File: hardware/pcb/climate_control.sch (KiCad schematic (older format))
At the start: 27 parts

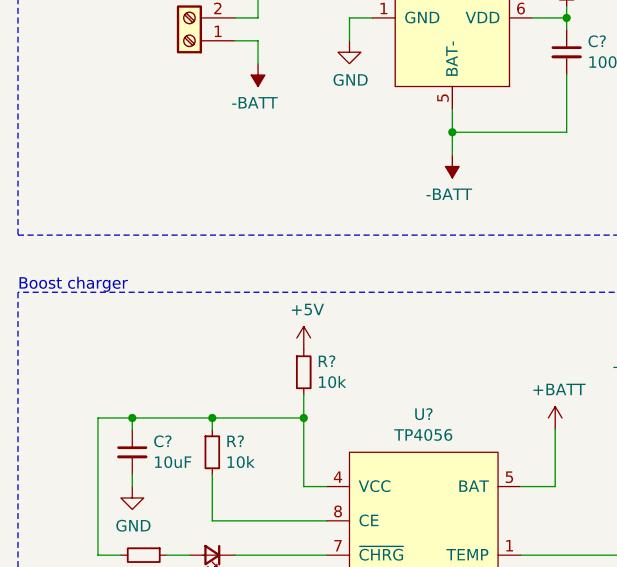
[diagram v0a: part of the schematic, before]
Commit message: Correct title on battery charger.
Wrote boost before, when it is a buck charger. Now corrected.
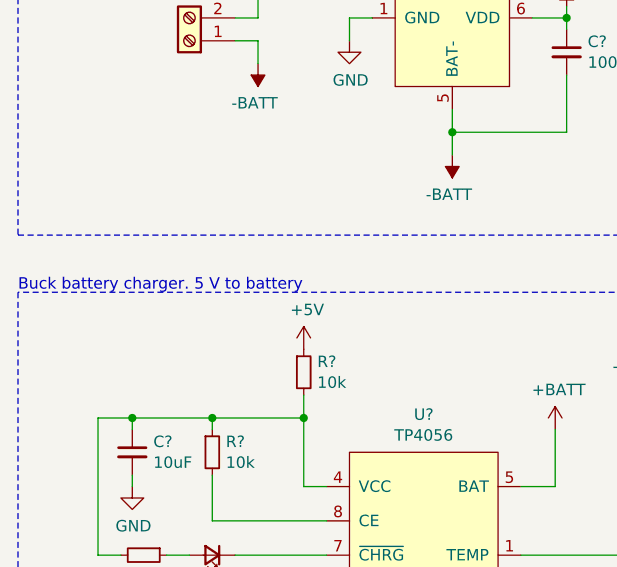
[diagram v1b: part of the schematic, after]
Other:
- note added: "Buck battery charger. 5 V to battery"
- note removed: "Boost charger"
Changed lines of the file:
@@
 	1200 3300 1550 3300
 Text Notes 700  2750 0    50   ~ 0
-Boost charger
+Buck battery charger. 5 V to battery
 Wire Notes Line
 	700  5100 700  7650

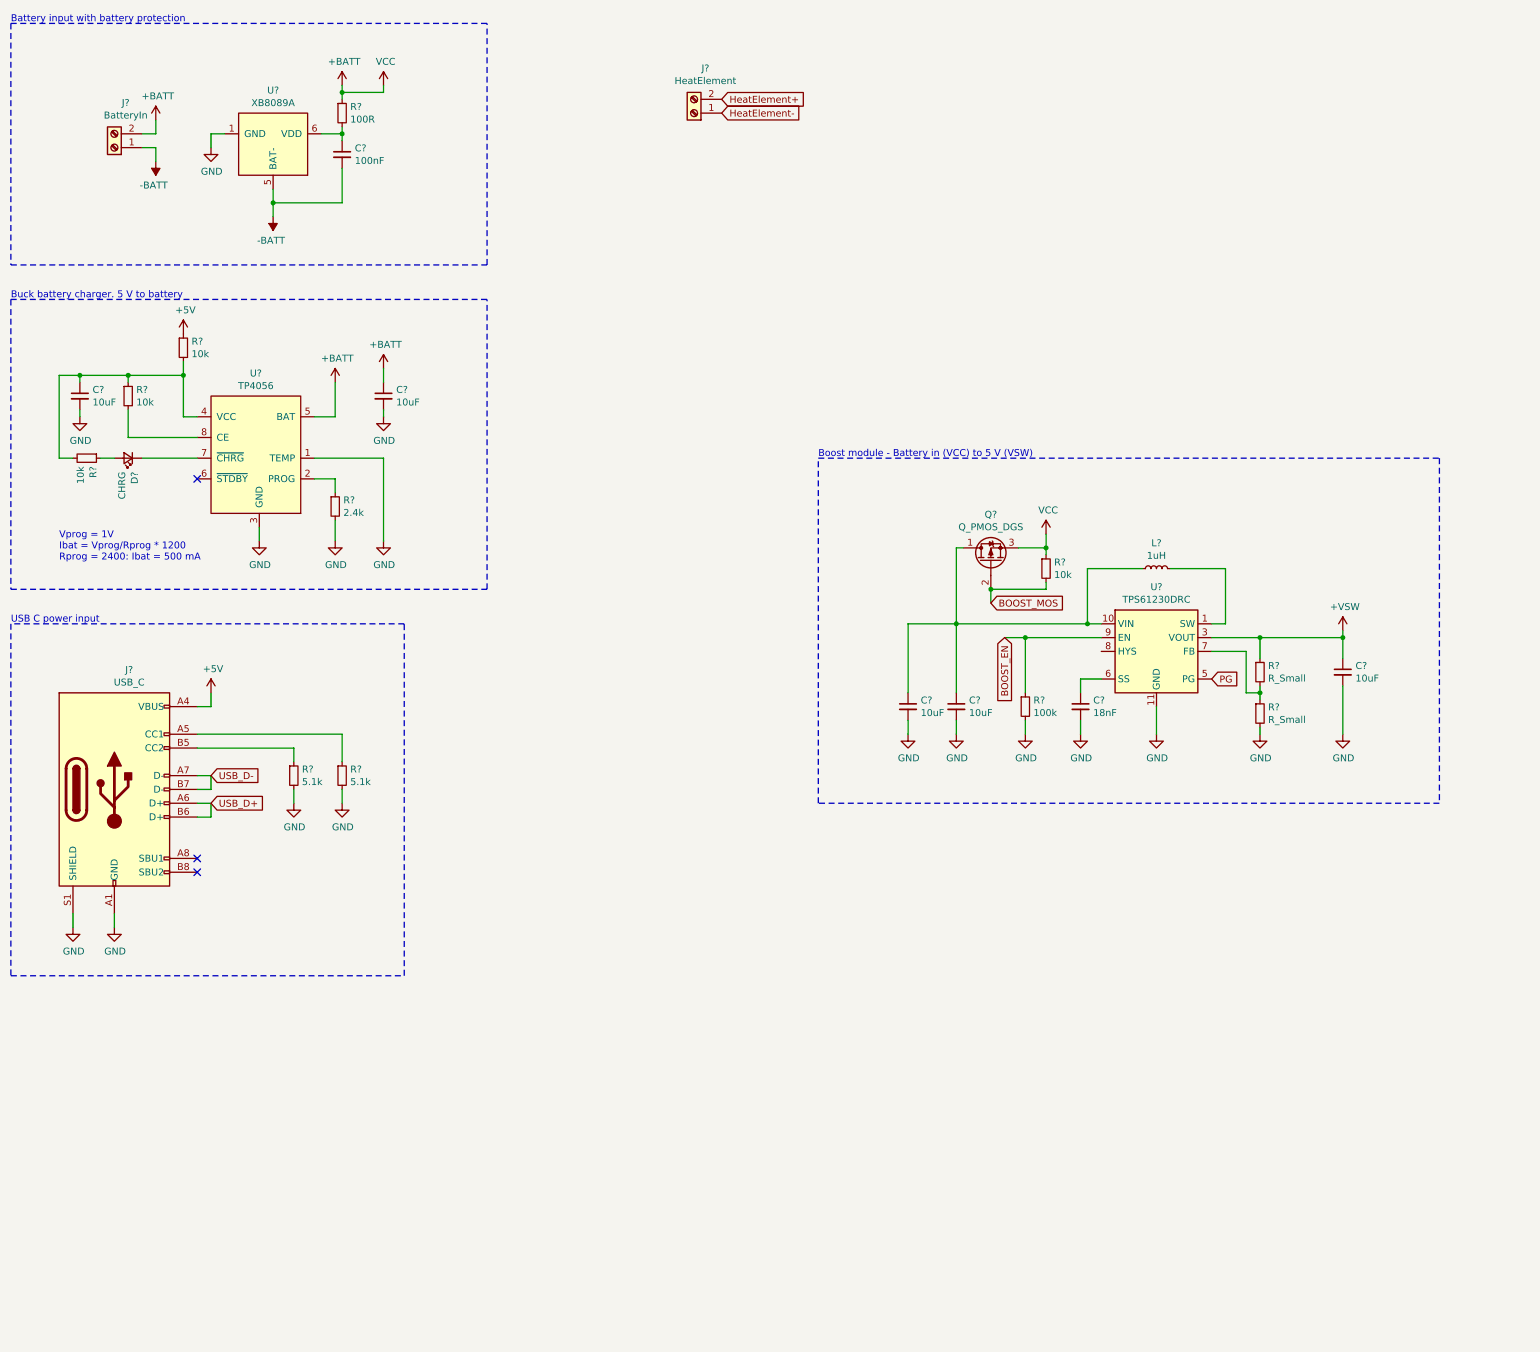
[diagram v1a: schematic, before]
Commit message: Added MCU and better control.
MCU with all connection is added.
Output to heater now has a mosfet to PWM to.
LED Switch has a connection with mosfet to control LED.
LED Switch has a LP filter for debounce purpose.
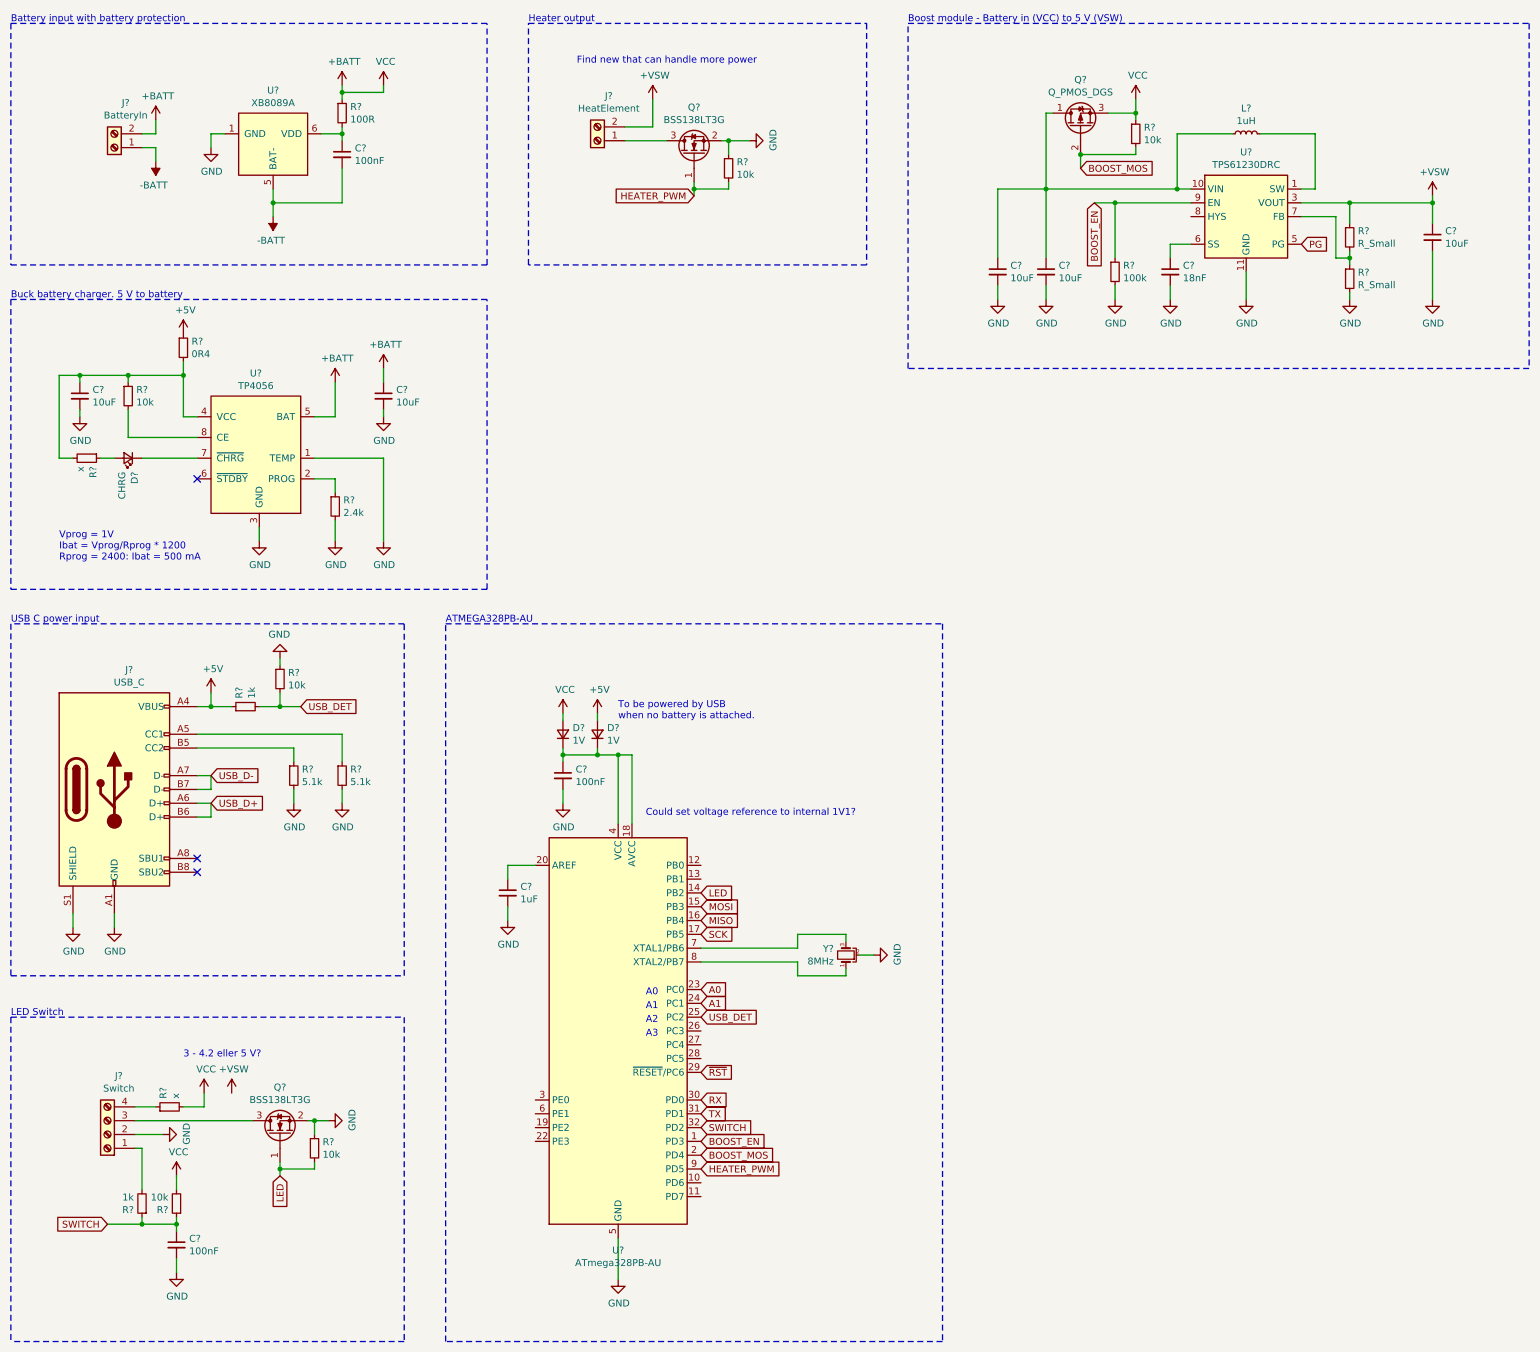
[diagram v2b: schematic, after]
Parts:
- added C? (x2): 100nF, symbol Device:C_Small
- added C?: 1uF, symbol Device:C_Small
- added D? (x2): 1V, symbol Device:D_Small
- added J?: Switch, symbol Connector:Screw_Terminal_01x04
- added Q? (x2): BSS138LT3G, symbol Device:Q_NMOS_GSD
- added R?: x, symbol Device:R_Small
- added R? (x4): 10k, symbol Device:R_Small
- added R? (x2): 1k, symbol Device:R_Small
- added U?: ATmega328PB-AU, Package_QFP:TQFP-32_7x7mm_P0.8mm, symbol climate_control:ATmega328PB-AU
- added Y?: 8MHz, symbol Device:Crystal_GND2_Small
- R?: value 10k -> x
- R?: value 10k -> 0R4
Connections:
- net HeatElement+ is gone; now on net +VSW: J?.2 (Pin_2)
- net +5V: now also D?.2 (A), R?.1
- net +BATT: now also D?.2 (A), R?.2, R?.2
- net BOOST_EN: now also U?.1 (PD3)
- net BOOST_MOS: now also U?.2 (PD4)
- net GND: now also C?.2, C?.2, C?.2, J?.2 (Pin_2), Q?.2 (S), Q?.2 (S), R?.1, R?.1, R?.1, U?.21 (GND), U?.5 (GND), Y?.2
- net HeatElement-: no longer names the net of J?.1 (Pin_1)
- net HeatElement-: now also Q?.3 (D)
- new net: C?.1, D?.1 (K), D?.1 (K), U?.18 (AVCC), U?.4 (VCC)
- new net: C?.1, U?.20 (AREF)
- new net: U?.7 (XTAL1/PB6), Y?.3
- new net: U?.8 (XTAL2/PB7), Y?.1
- new net: J?.1 (Pin_1), R?.2
- new net: J?.3 (Pin_3), Q?.3 (D)
- new net: J?.4 (Pin_4), R?.1
- new net A0: U?.23 (PC0)
- new net A1: U?.24 (PC1)
- new net HEATER_PWM: Q?.1 (G), R?.2, U?.9 (PD5)
- new net LED: Q?.1 (G), R?.2, U?.14 (PB2)
- new net MISO: U?.16 (PB4)
- new net MOSI: U?.15 (PB3)
- new net RX: U?.30 (PD0)
- new net SCK: U?.17 (PB5)
- new net SWITCH: C?.1, R?.1, R?.1, U?.32 (PD2)
- new net TX: U?.31 (PD1)
- new net USB_DET: R?.2, R?.2, U?.25 (PC2)
- new net ~RST: U?.29 (~RESET~/PC6)
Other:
- note added: "3 - 4.2 eller 5 V?"
- note added: "A0"
- note added: "A1"
- note added: "A2"
- note added: "A3"
- note added: "ATMEGA328PB-AU"
- note added: "Could set voltage reference to internal 1V1?"
- note added: "Find new that can handle more power"
- note added: "Heater output"
- note added: "LED Switch"
- note added: "To be powered by USB \nwhen no battery is attached."
- moved on the sheet: C?, J?, L?, Q?, R?, U?

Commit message: All components added to schematic and pcb.
Footprints for all parts is done and only routing is left.
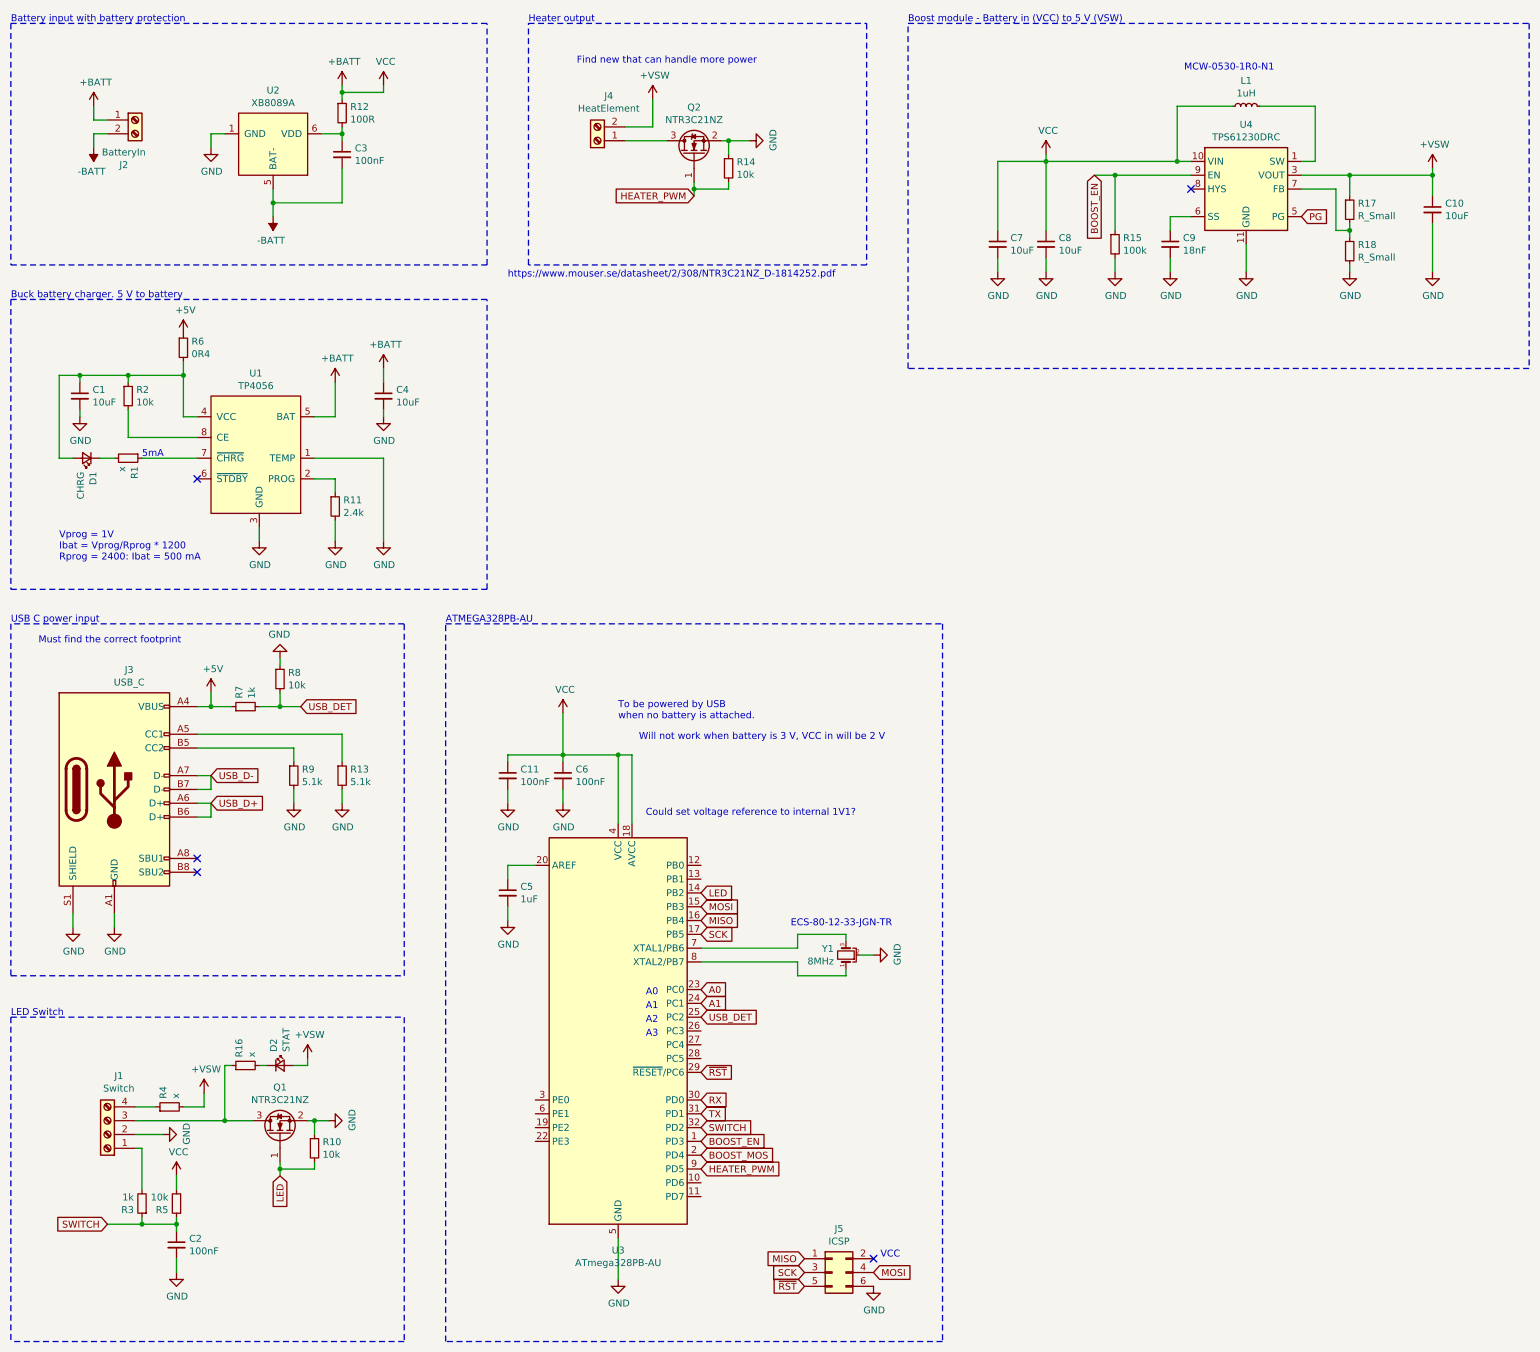
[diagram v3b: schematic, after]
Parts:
- removed D? (x2): 1V, symbol Device:D_Small
- removed Q?: Q_PMOS_DGS, symbol Device:Q_PMOS_DGS
- removed R?: 10k, symbol Device:R_Small
- added C11: 100nF, Capacitor_SMD:C_0402_1005Metric, symbol Device:C_Small
- added D2: STAT, Diode_SMD:D_0603_1608Metric, symbol Device:LED_Small
- added J5: ICSP, Connector_PinHeader_2.54mm:PinHeader_2x03_P2.54mm_Vertical, symbol Connector_Generic:Conn_02x03_Odd_Even
- added R16: x, Resistor_SMD:R_0402_1005Metric, symbol Device:R_Small
- C1, C10, C4, C7, C8: renamed from C?; footprint (none) -> Capacitor_SMD:C_0603_1608Metric
- C2, C3, C5, C6, C9: renamed from C?; footprint (none) -> Capacitor_SMD:C_0402_1005Metric
- D1: renamed from D?; footprint (none) -> Diode_SMD:D_0603_1608Metric
- J1: renamed from J?; footprint (none) -> Connector_JST:JST_XH_B4B-XH-A_1x04_P2.50mm_Vertical
- J2, J4: renamed from J?; footprint (none) -> Connector_JST:JST_XH_B2B-XH-A_1x02_P2.50mm_Vertical
- J3: renamed from J?; footprint (none) -> climate_control:HRO_TYPE-C-31-M-12
- L1: renamed from L?; footprint (none) -> climate_control:Inductor_0530
- Q1, Q2: renamed from Q?; value BSS138LT3G -> NTR3C21NZ; footprint (none) -> Package_TO_SOT_SMD:SOT-23
- R1, R10, R11, R12, R13, R14, R15, R17, R18, R2, R3, R4, R5, R7, R8, R9: renamed from R?; footprint (none) -> Resistor_SMD:R_0402_1005Metric
- U1, U2: renamed from U?; footprint (none) -> climate_control:SOP8-EPAD
- Y1: renamed from Y?; footprint (none) -> climate_control:ECX-32
- gave numbers to parts that had none: 3
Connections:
- net +BATT: now also C6.1, C7.1, C8.1, J2.1 (Pin_1), L1.1, U3.18 (AVCC), U3.4 (VCC), U4.10 (VIN), C11.1; no longer J2.2 (Pin_2), R4.2
- net +VSW: now also R4.2, D2.2 (A)
- net -BATT: now also J2.2 (Pin_2); no longer J2.1 (Pin_1)
- net GND: now also C11.2, J5.6 (Pin_6)
- net MISO: now also J5.1 (Pin_1)
- net MOSI: now also J5.4 (Pin_4)
- net SCK: now also J5.3 (Pin_3)
- net ~RST: now also J5.5 (Pin_5)
- net at C1.1, R2.1, R6.2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: now also D1.2 (A); no longer R1.2
- net at U1.7 (~CHRG): now also R1.1; no longer D1.1 (K)
- net at J1.3 (Pin_3), Q1.3 (D): now also R16.1
- new net: D2.1 (K), R16.2
- new net: D1.1 (K), R1.2
- no-connect marks 3 -> 5
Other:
- note added: "5mA"
- note added: "ECS-80-12-33-JGN-TR"
- note added: "MCW-0530-1R0-N1"
- note added: "Must find the correct footprint"
- note added: "VCC"
- note added: "Will not work when battery is 3 V, VCC in will be 2 V"
- note added: "https://www.mouser.se/datasheet/2/308/NTR3C21NZ_D-1814252.pdf"
- note removed: "3 - 4.2 eller 5 V?"
- moved on the sheet: C10, C7, C8, C9, D1, J2, L1, R1, R15, R17, R18, U4

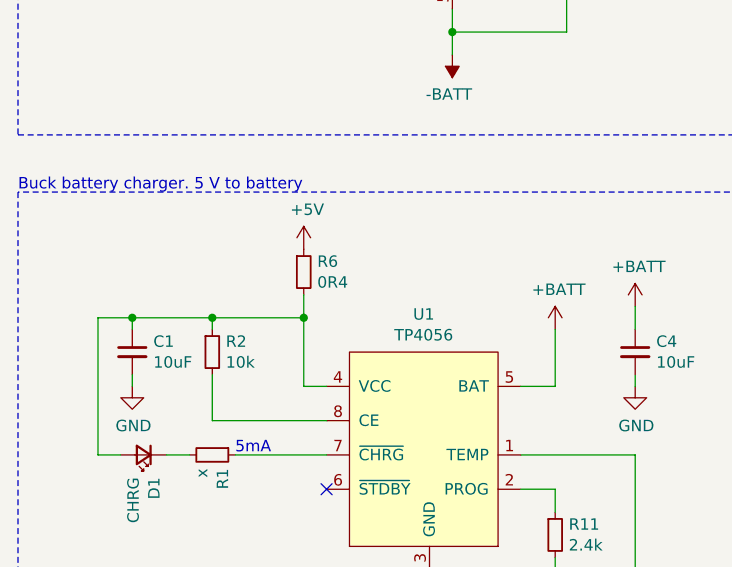
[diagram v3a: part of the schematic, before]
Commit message: Removed resistor on TP4056.
Updated on PCB the routing.
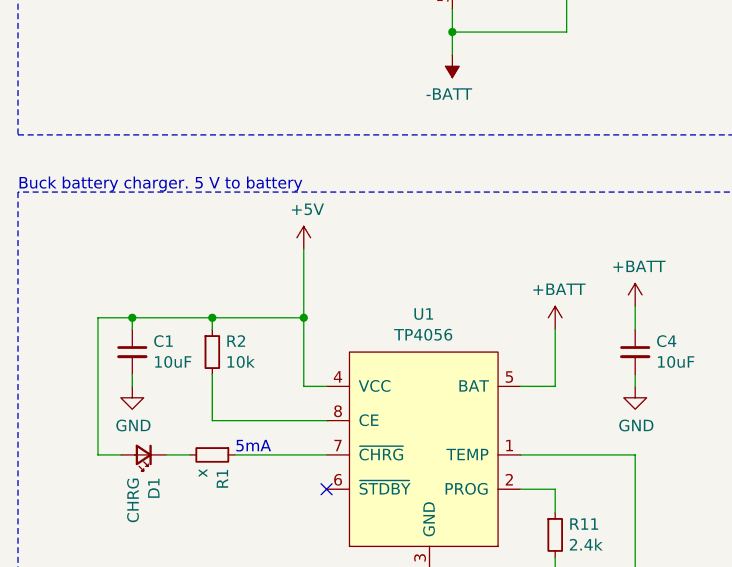
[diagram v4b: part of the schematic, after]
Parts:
- removed R6: 0R4, symbol Device:R_Small
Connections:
- net +5V: now also C1.1, D1.2 (A), R2.1, U1.4 (VCC)
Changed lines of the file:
@@
 Text Notes 1050 4650 0    50   ~ 0
 Vprog = 1V\nIbat = Vprog/Rprog * 1200\nRprog = 2400: Ibat = 500 mA
-$Comp
-L Device:R_Small R6
-U 1 1 6040DBAC
-P 1950 3100
-F 0 "R6" H 2009 3146 50  0000 L CNN
-F 1 "0R4" H 2009 3055 50  0000 L CNN
-F 2 "" H 1950 3100 50  0001 C CNN
-F 3 "~" H 1950 3100 50  0001 C CNN
-	1    1950 3100
-	1    0    0    -1
-$EndComp
-Wire Wire Line
-	1950 3300 1950 3200
 Wire Wire Line
 	1950 3300 1950 3600
@@
 Text Notes 9200 1100 0    50   ~ 0
 	MCW-0530-1R0-N1
+Wire Wire Line
+	1950 3000 1950 3300
 $EndSCHEMATC
